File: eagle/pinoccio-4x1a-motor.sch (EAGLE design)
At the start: 3 parts

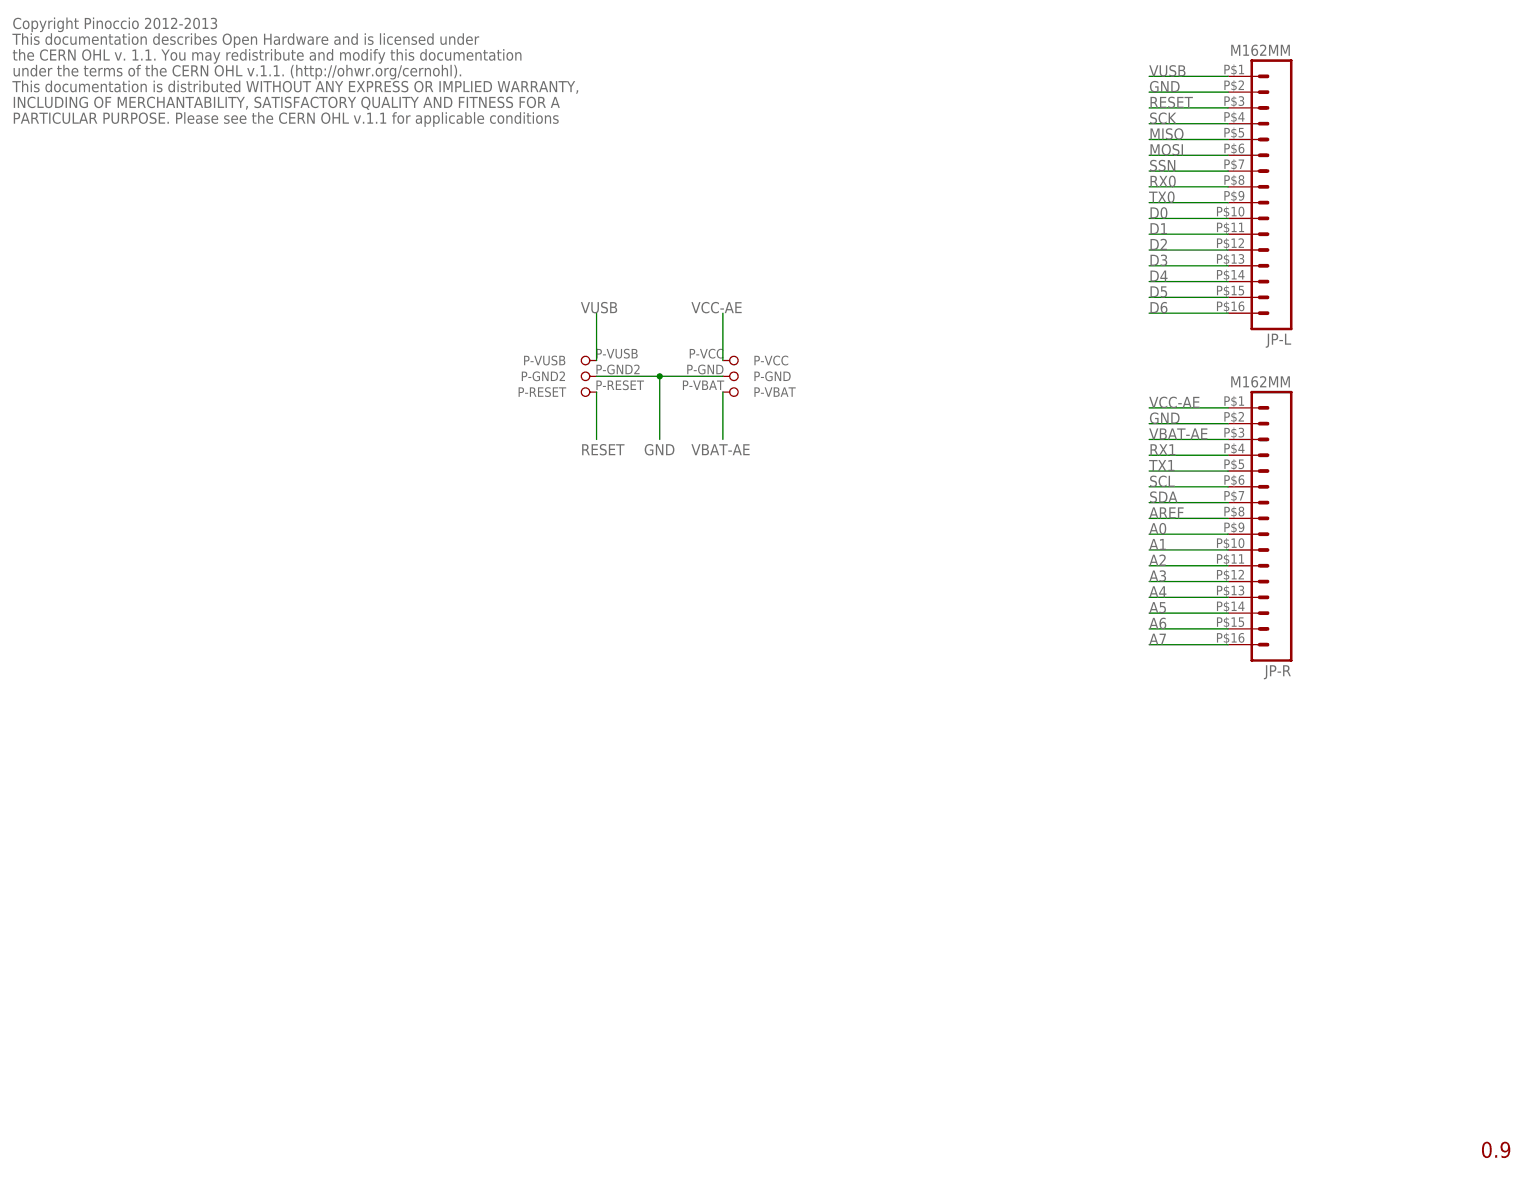
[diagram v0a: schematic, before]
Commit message: First commit of new shield.
Main components added, no signals.
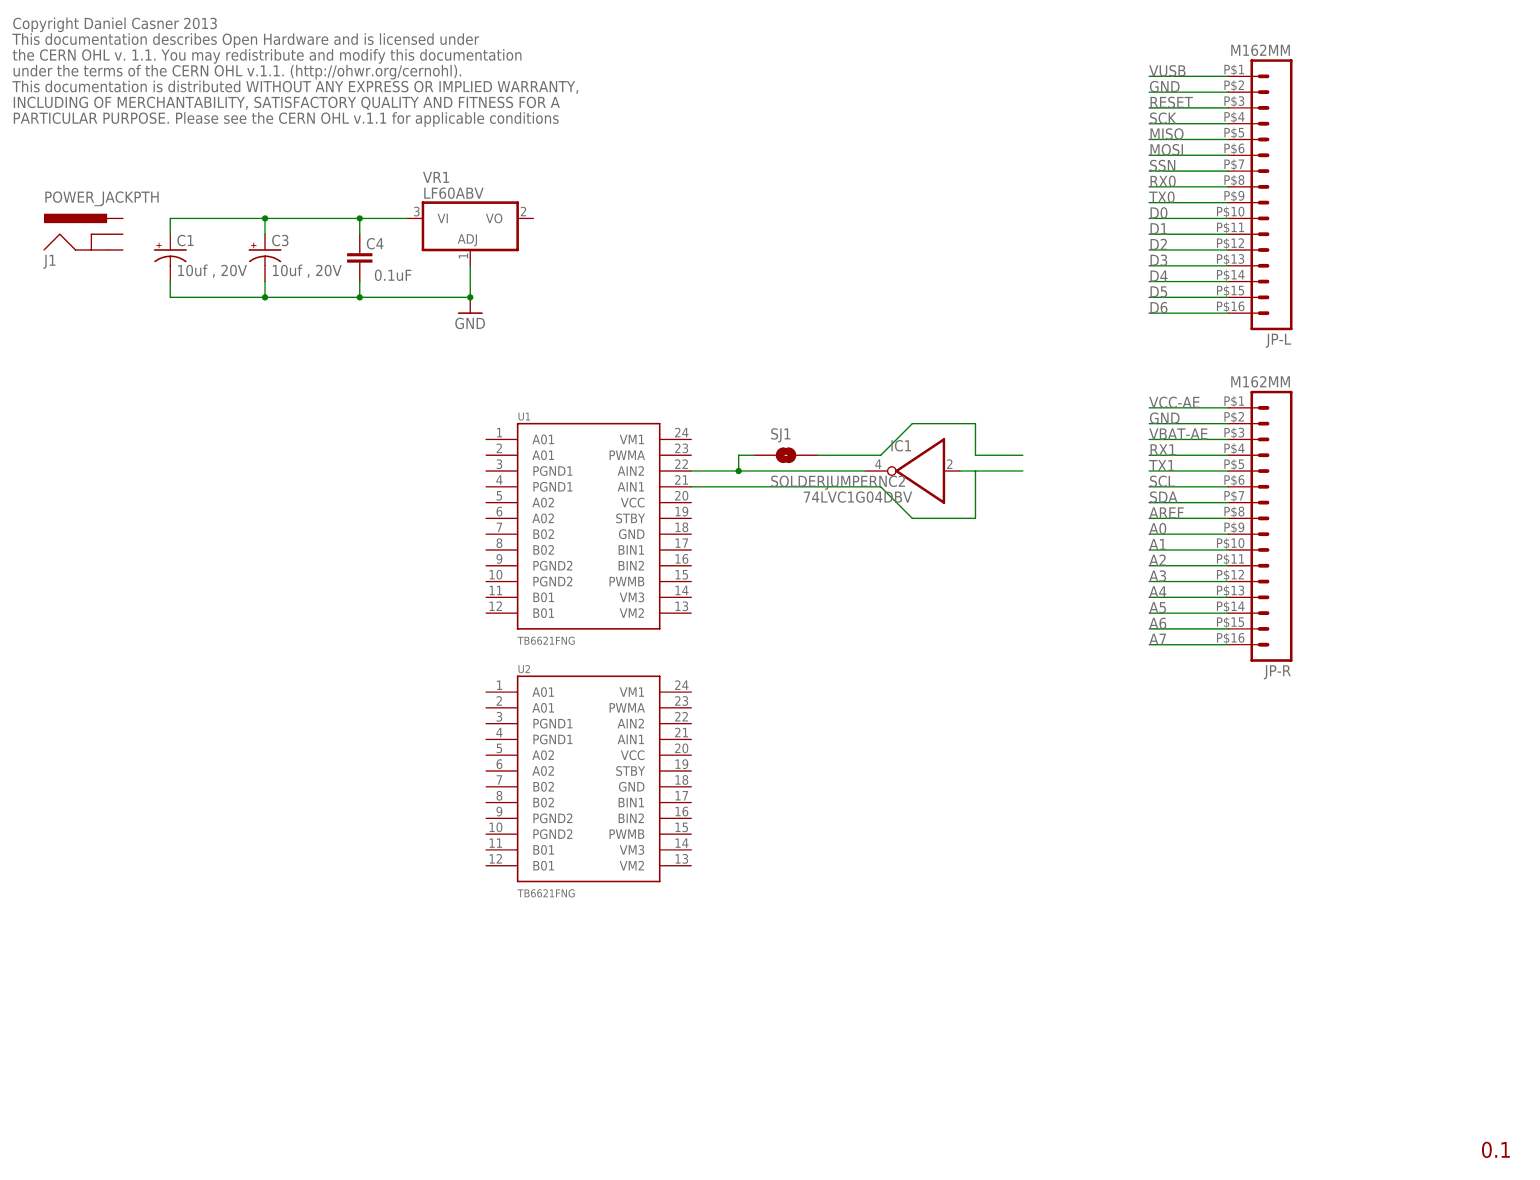
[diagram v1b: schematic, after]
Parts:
- removed U$1: PROTO, Pinoccio:PROTO
- added C1, C3: 10uf , 20V, SparkFun:CAP_POL3528
- added C4: 0.1uF, SparkFun:CAP0402-CAP
- added IC1: 74LVC1G04DBV, 74xx-little-de:74LVC1G04DBV
- added J1: POWER_JACKPTH, SparkFun-Connectors:POWER_JACKPTH
- added SJ1: SOLDERJUMPERNC2, SparkFun-Passives:SOLDERJUMPERNC2
- added U1, U2: TB6621FNG, SparkFun:TB6621FNG
- added VR1: LF60ABV, linear:317T
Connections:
- new net N$1: C1.+, C3.+, C4.2, VR1.VI
- new net N$2: IC1A.I, U1.AIN1
- new net N$3: IC1A.O, SJ1.1, U1.AIN2
- new net N$4: SJ1.2
- net GND: now also C1.-, C3.-, C4.1, VR1.ADJ; no longer U$1.P$53, U$1.P$77, U$1.P-GND, U$1.P-GND2
- net RESET: no longer U$1.P-RESET
- net VBAT-AE: no longer U$1.P-VBAT
- net VCC-AE: no longer U$1.P-VCC
- net VUSB: no longer U$1.P-VUSB
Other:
- note added: "0.1"
- note added: "Copyright Daniel Casner 2013"
- note removed: "0.9"
- note removed: "Copyright Pinoccio 2012-2013"
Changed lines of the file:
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@@
 <?xml version="1.0" encoding="utf-8"?>
 <!DOCTYPE eagle SYSTEM "eagle.dtd">
-<eagle version="6.2">
+<eagle version="6.4">
 <drawing>
 <settings>
@@
 <part name="JP-R" library="Pinoccio" deviceset="M16" device="2MM"/>
 <part name="JP-L" library="Pinoccio" deviceset="M16" device="2MM"/>
-<part name="U$1" library="Pinoccio" deviceset="PROTO" device=""/>
+<part name="U1" library="SparkFun" deviceset="TB6621FNG" device=""/>
+<part name="U2" library="SparkFun" deviceset="TB6621FNG" device=""/>
+<part name="VR1" library="linear" deviceset="*317" device="T" value="LF60ABV"/>
+<part name="C4" library="SparkFun" deviceset="CAP" device="0402-CAP" value="0.1uF"/>
+<part name="C3" library="SparkFun" deviceset="CAP_POL" device="3528" value="10uf , 20V"/>
+<part name="IC1" library="74xx-little-de" deviceset="74*1G04" device="DBV" technology="LVC"/>
+<part name="C1" library="SparkFun" deviceset="CAP_POL" device="3528" value="10uf , 20V"/>
+<part name="GND1" library="SparkFun-Aesthetics" deviceset="GND" device=""/>
+<part name="J1" library="SparkFun-Connectors" deviceset="POWER_JACK" device="PTH"/>
+<part name="SJ1" library="SparkFun-Passives" deviceset="SOLDERJUMPER" device="NC2"/>
 </parts>
 <sheets>
 <sheet>
 <plain>
-<text x="238.76" y="1.27" size="2.54" layer="94" font="vector">0.9</text>
+<text x="238.76" y="1.27" size="2.54" layer="94" font="vector">0.1</text>
 <rectangle x1="0.38735" y1="0.29845" x2="0.41275" y2="0.31115" layer="21"/>
 <rectangle x1="0.36195" y1="0.31115" x2="0.45085" y2="0.32385" layer="21"/>
@@
 <text x="0" y="-0.127" size="0.0508" layer="21" font="vector">/Volumes/Data/Users/eric/Desktop/pinoccio-full-3-4in.bmp</text>
 <text x="0" y="-0.127" size="0.0508" layer="200" font="vector">/Volumes/Data/Users/eric/Desktop/pinoccio-full-3-4in.bmp</text>
-<text x="2.54" y="182.88" size="1.778" layer="95">Copyright Pinoccio 2012-2013</text>
+<text x="2.54" y="182.88" size="1.778" layer="95">Copyright Daniel Casner 2013</text>
 <text x="2.54" y="180.34" size="1.778" layer="95">This documentation describes Open Hardware and is licensed under</text>
 <text x="2.54" y="177.8" size="1.778" layer="95">the CERN OHL v. 1.1. You may redistribute and modify this documentation </text>
@@
 <instance part="JP-R" gate="G$1" x="208.28" y="101.6" rot="R180"/>
 <instance part="JP-L" gate="G$1" x="208.28" y="154.94" rot="R180"/>
-<instance part="U$1" gate="G$1" x="101.6" y="93.98"/>
+<instance part="U1" gate="G$1" x="96.52" y="104.14"/>
+<instance part="U2" gate="G$1" x="96.52" y="63.5"/>
+<instance part="VR1" gate="A1" x="76.2" y="149.86"/>
+<instance part="C4" gate="G$1" x="58.42" y="147.32" smashed="yes" rot="R180">
+<attribute name="NAME" x="59.436" y="147.447" size="1.778" layer="95"/>
+<attribute name="VALUE" x="60.706" y="142.367" size="1.778" layer="96"/>
+</instance>
+<instance part="C3" gate="G$1" x="43.18" y="147.32" smashed="yes">
+<attribute name="NAME" x="44.196" y="147.955" size="1.778" layer="95"/>
+<attribute name="VALUE" x="44.196" y="143.129" size="1.778" layer="96"/>
+</instance>
+<instance part="IC1" gate="A" x="149.86" y="111.76" rot="MR0"/>
+<instance part="C1" gate="G$1" x="27.94" y="147.32" smashed="yes">
+<attribute name="NAME" x="28.956" y="147.955" size="1.778" layer="95"/>
+<attribute name="VALUE" x="28.956" y="143.129" size="1.778" layer="96"/>
+</instance>
+<instance part="GND1" gate="1" x="76.2" y="137.16"/>
+<instance part="J1" gate="G$1" x="17.78" y="144.78"/>
+<instance part="SJ1" gate="1" x="127" y="114.3"/>
 </instances>
 <busses>
@@
 </segment>
 <segment>
-<pinref part="U$1" gate="G$1" pin="P-GND"/>
-<pinref part="U$1" gate="G$1" pin="P-GND2"/>
-<wire x1="116.84" y1="127" x2="106.68" y2="127" width="0.1524" layer="91"/>
-<pinref part="U$1" gate="G$1" pin="P$77"/>
-<wire x1="96.52" y1="127" x2="106.68" y2="127" width="0.1524" layer="91"/>
-<pinref part="U$1" gate="G$1" pin="P$53"/>
-<wire x1="106.68" y1="127" x2="106.68" y2="116.84" width="0.1524" layer="91"/>
-<junction x="106.68" y="127"/>
-<label x="104.14" y="114.3" size="1.778" layer="95"/>
+<pinref part="C4" gate="G$1" pin="1"/>
+<wire x1="58.42" y1="142.24" x2="58.42" y2="139.7" width="0.1524" layer="91"/>
+<pinref part="VR1" gate="A1" pin="ADJ"/>
+<wire x1="58.42" y1="139.7" x2="76.2" y2="139.7" width="0.1524" layer="91"/>
+<wire x1="76.2" y1="139.7" x2="76.2" y2="144.78" width="0.1524" layer="91"/>
+<pinref part="C3" gate="G$1" pin="-"/>
+<wire x1="43.18" y1="142.24" x2="43.18" y2="139.7" width="0.1524" layer="91"/>
+<wire x1="43.18" y1="139.7" x2="58.42" y2="139.7" width="0.1524" layer="91"/>
+<pinref part="C1" gate="G$1" pin="-"/>
+<wire x1="27.94" y1="142.24" x2="27.94" y2="139.7" width="0.1524" layer="91"/>
+<wire x1="27.94" y1="139.7" x2="43.18" y2="139.7" width="0.1524" layer="91"/>
+<junction x="43.18" y="139.7"/>
+<junction x="58.42" y="139.7"/>
+<pinref part="GND1" gate="1" pin="GND"/>
+<junction x="76.2" y="139.7"/>
 </segment>
 </net>
@@
 <label x="185.42" y="175.26" size="1.778" layer="95"/>
 </segment>
-<segment>
-<pinref part="U$1" gate="G$1" pin="P-VUSB"/>
-<wire x1="96.52" y1="129.54" x2="96.52" y2="137.16" width="0.1524" layer="91"/>
-<label x="93.98" y="137.16" size="1.778" layer="95"/>
-</segment>
 </net>
 <net name="VBAT-AE" class="0">
@@
 <label x="185.42" y="116.84" size="1.778" layer="95"/>
 </segment>
-<segment>
-<pinref part="U$1" gate="G$1" pin="P-VBAT"/>
-<wire x1="116.84" y1="124.46" x2="116.84" y2="116.84" width="0.1524" layer="91"/>
-<label x="111.76" y="114.3" size="1.778" layer="95"/>
-</segment>
 </net>
 <net name="SSN" class="0">
@@
 <label x="185.42" y="170.18" size="1.778" layer="95"/>
 </segment>
-<segment>
-<pinref part="U$1" gate="G$1" pin="P-RESET"/>
-<wire x1="96.52" y1="124.46" x2="96.52" y2="116.84" width="0.1524" layer="91"/>
-<label x="93.98" y="114.3" size="1.778" layer="95"/>
-</segment>
 </net>
 <net name="A0" class="0">
@@
 <label x="185.42" y="121.92" size="1.778" layer="95"/>
 </segment>
+</net>
+<net name="N$1" class="0">
 <segment>
-<pinref part="U$1" gate="G$1" pin="P-VCC"/>
-<wire x1="116.84" y1="129.54" x2="116.84" y2="137.16" width="0.1524" layer="91"/>
-<label x="111.76" y="137.16" size="1.778" layer="95"/>
+<pinref part="VR1" gate="A1" pin="VI"/>
+<pinref part="C4" gate="G$1" pin="2"/>
+<wire x1="66.04" y1="152.4" x2="58.42" y2="152.4" width="0.1524" layer="91"/>
+<wire x1="58.42" y1="152.4" x2="58.42" y2="149.86" width="0.1524" layer="91"/>
+<pinref part="C3" gate="G$1" pin="+"/>
+<wire x1="58.42" y1="152.4" x2="43.18" y2="152.4" width="0.1524" layer="91"/>
+<wire x1="43.18" y1="152.4" x2="43.18" y2="149.86" width="0.1524" layer="91"/>
+<pinref part="C1" gate="G$1" pin="+"/>
+<wire x1="43.18" y1="152.4" x2="27.94" y2="152.4" width="0.1524" layer="91"/>
+<wire x1="27.94" y1="152.4" x2="27.94" y2="149.86" width="0.1524" layer="91"/>
+<junction x="43.18" y="152.4"/>
+<junction x="58.42" y="152.4"/>
+</segment>
+</net>
+<net name="N$3" class="0">
+<segment>
+<pinref part="U1" gate="G$1" pin="AIN2"/>
+<pinref part="IC1" gate="A" pin="O"/>
+<wire x1="139.7" y1="111.76" x2="119.38" y2="111.76" width="0.1524" layer="91"/>
+<pinref part="SJ1" gate="1" pin="1"/>
+<wire x1="119.38" y1="111.76" x2="111.76" y2="111.76" width="0.1524" layer="91"/>
+<wire x1="121.92" y1="114.3" x2="119.38" y2="114.3" width="0.1524" layer="91"/>
+<wire x1="119.38" y1="114.3" x2="119.38" y2="111.76" width="0.1524" layer="91"/>
+<junction x="119.38" y="111.76"/>
+</segment>
+</net>
+<net name="N$2" class="0">
+<segment>
+<pinref part="U1" gate="G$1" pin="AIN1"/>
+<wire x1="111.76" y1="109.22" x2="142.24" y2="109.22" width="0.1524" layer="91"/>
+<wire x1="142.24" y1="109.22" x2="147.32" y2="104.14" width="0.1524" layer="91"/>
+<wire x1="147.32" y1="104.14" x2="157.48" y2="104.14" width="0.1524" layer="91"/>
+<wire x1="157.48" y1="104.14" x2="157.48" y2="111.76" width="0.1524" layer="91"/>
+<pinref part="IC1" gate="A" pin="I"/>
+<wire x1="157.48" y1="111.76" x2="154.94" y2="111.76" width="0.1524" layer="91"/>
+<wire x1="157.48" y1="111.76" x2="165.1" y2="111.76" width="0.1524" layer="91"/>
+</segment>
+</net>
+<net name="N$4" class="0">
+<segment>
+<pinref part="SJ1" gate="1" pin="2"/>
+<wire x1="132.08" y1="114.3" x2="142.24" y2="114.3" width="0.1524" layer="91"/>
+<wire x1="142.24" y1="114.3" x2="147.32" y2="119.38" width="0.1524" layer="91"/>
+<wire x1="147.32" y1="119.38" x2="157.48" y2="119.38" width="0.1524" layer="91"/>
+<wire x1="157.48" y1="119.38" x2="157.48" y2="114.3" width="0.1524" layer="91"/>
+<wire x1="157.48" y1="114.3" x2="165.1" y2="114.3" width="0.1524" layer="91"/>
 </segment>
 </net>
